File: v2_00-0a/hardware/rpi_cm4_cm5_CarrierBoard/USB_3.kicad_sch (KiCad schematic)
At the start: 90 parts, among them J2 0484050003, J3 0484050003, U5 UPD720202K8-711-BAA-A, U6 SST25VF512A, U7 UPD720202K8-711-BAA-A, U8 AP2192AFGEG-7, Y1 24MHz

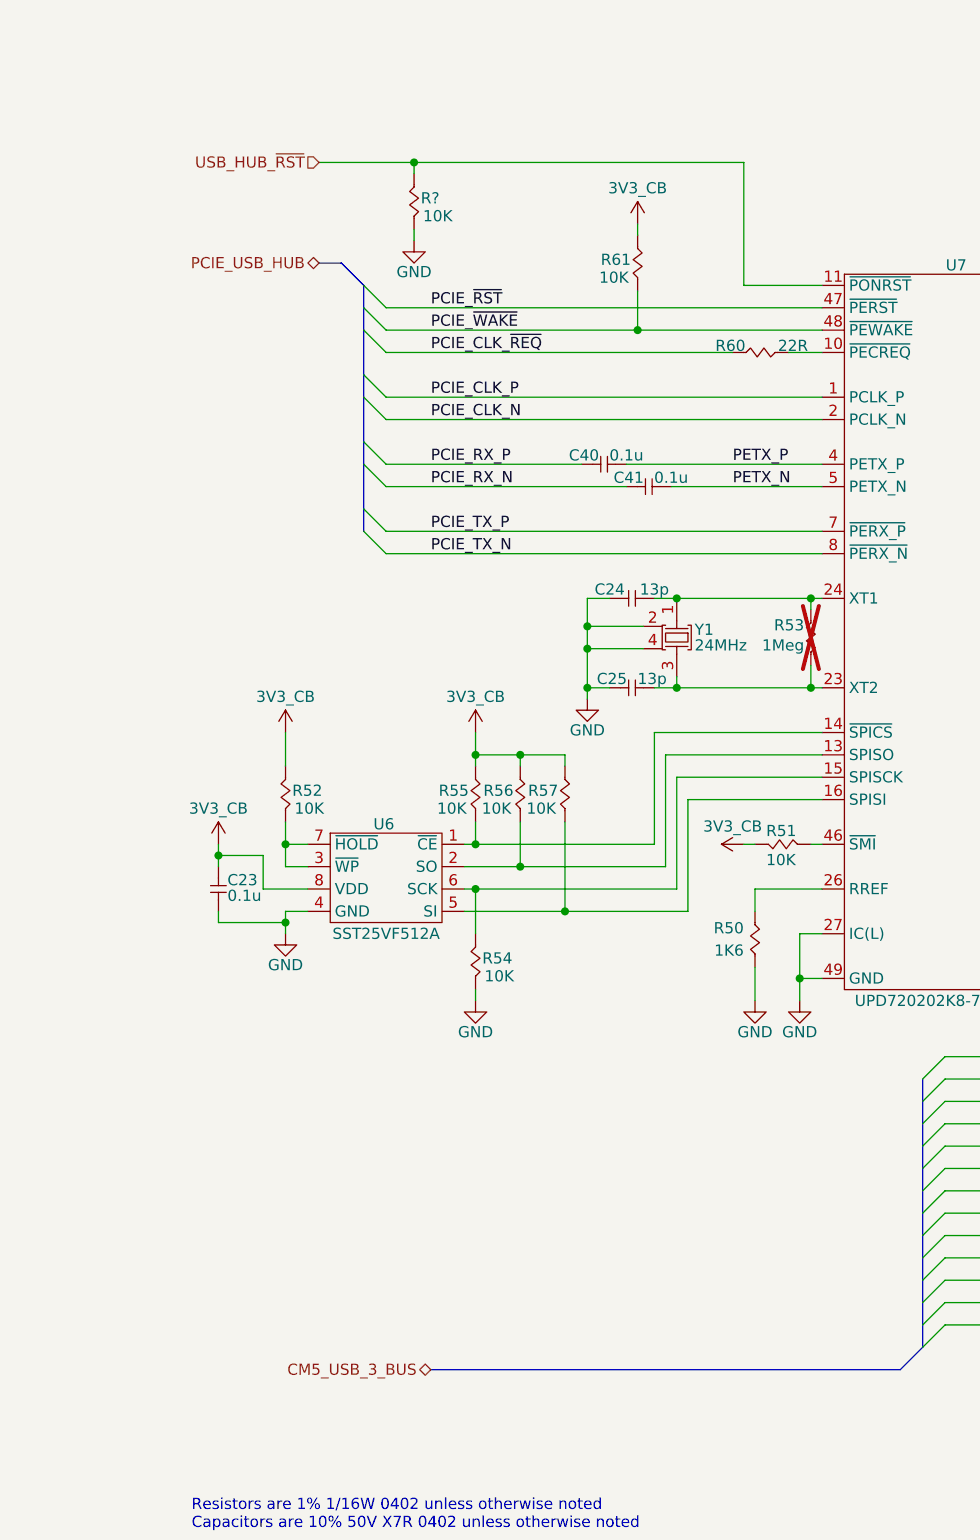
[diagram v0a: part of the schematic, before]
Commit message: Add schematic pages for SOM_CONN_A/B, DSI to LVDS bridge, Ethernet and HDMI
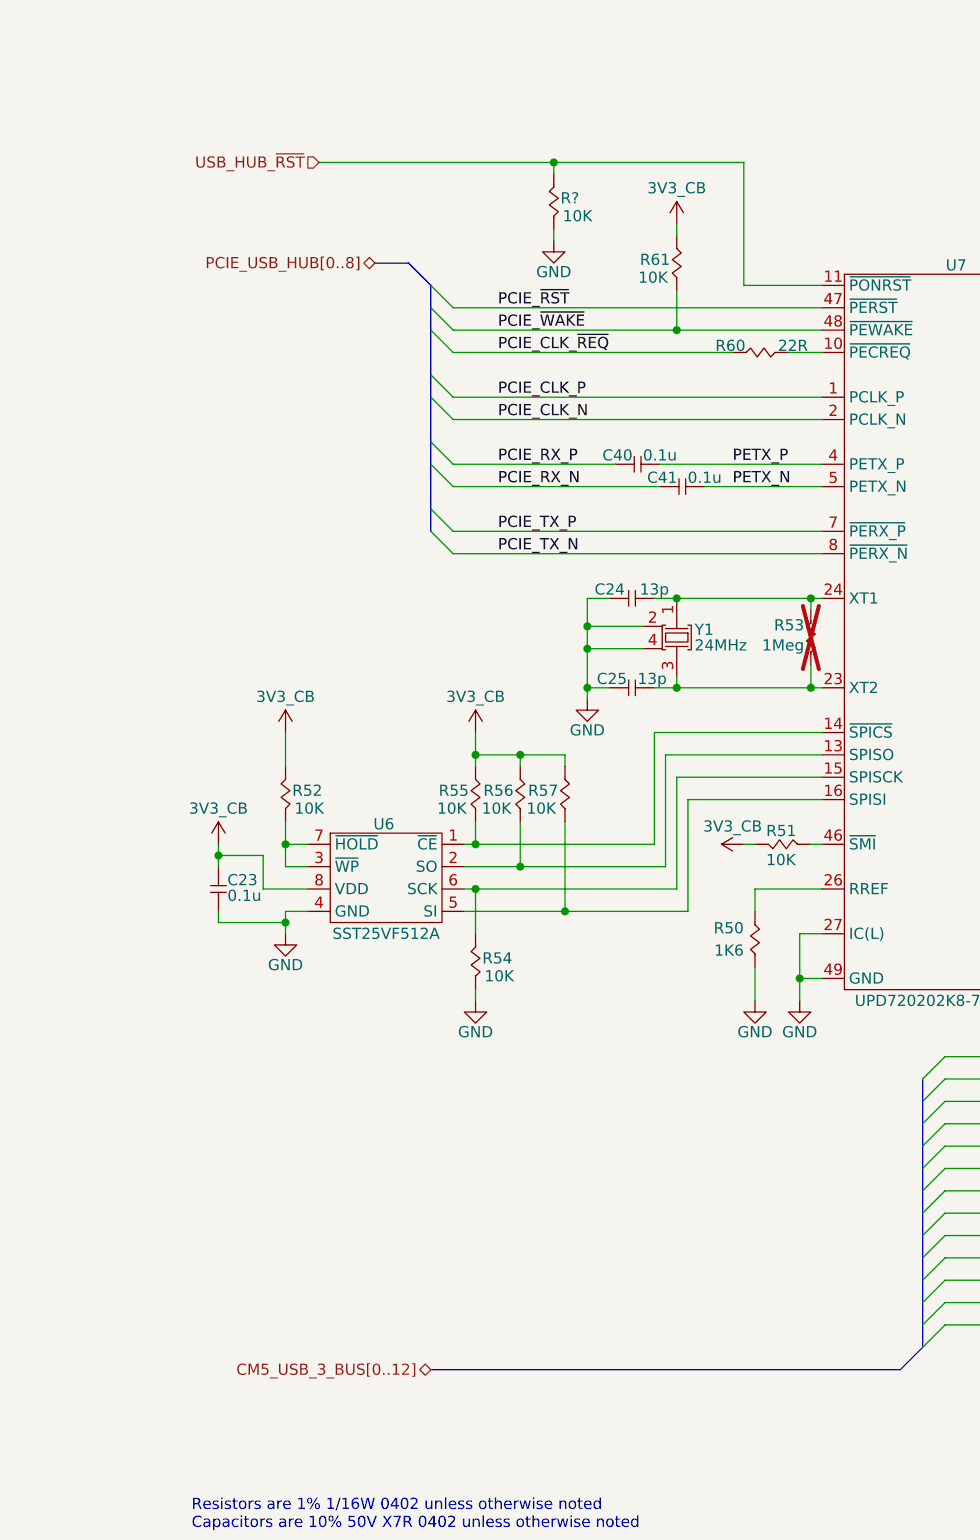
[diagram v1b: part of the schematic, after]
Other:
- moved on the sheet: C40, C41, R61, R?

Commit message: Update schematics (several new hierarchical pages, updates bus labels)
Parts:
- removed U5: UPD720202K8-711-BAA-A, footprint:48-VFQFN-EP, symbol KicadCompDb:Interface/INTRFX_00002
- added R128, R44: 0R, footprint:RES_0402, symbol KicadCompDb:Resistors/RES_SMT_00001
- gave numbers to parts that had none: 2
- renumbered R44 to R127
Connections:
- net CM5_USB3_VBUS_EN: now also R44.1; no longer R127.1
- net at R27.2, R49.1, U8.5 (FLG2): now also R128.2
- net at R26.2, R46.2, U8.3 (EN1): now also R44.2; no longer R127.2
- net at R25.2, R48.1, U8.8 (FLG1): now also R127.2
- net CM5_USB2_D1_N renamed CM5_USB3_0.USB_N
- net CM5_USB2_D1_P renamed CM5_USB3_0.USB_P
- net CM5_USB2_D2_N renamed CM5_USB3_1.USB_N
- net CM5_USB2_D2_P renamed CM5_USB3_1.USB_P
- net CM5_USB3_RX1_N renamed CM5_USB3_0.U3RXD_N
- net CM5_USB3_RX1_P renamed CM5_USB3_0.U3RXD_P
- net CM5_USB3_RX2_N renamed CM5_USB3_1.U3RXD_N
- net CM5_USB3_RX2_P renamed CM5_USB3_1.U3RXD_P
- net CM5_USB3_TX2_N renamed CM5_USB3_1.U3TXD_N
- net CM5_USB3_TX2_P renamed CM5_USB3_1.U3TXD_P
- net CM5_USB3_U3TX1_N renamed CM5_USB3_0.U3TXD_N
- net CM5_USB3_U3TX1_P renamed CM5_USB3_0.U3TXD_P
- net CONN_USB3_D1_N renamed USB3_0.USB_N
- net CONN_USB3_D1_P renamed USB3_0.USB_P
- net CONN_USB3_D2_N renamed USB3_1.USB_N
- net CONN_USB3_D2_P renamed USB3_1.USB_P
- net CONN_USB3_RX1_N renamed USB3_0.U3RXD_N
- net CONN_USB3_RX1_P renamed USB3_0.U3RXD_P
- net CONN_USB3_RX2_N renamed USB3_1.U3RXD_N
- net CONN_USB3_RX2_P renamed USB3_1.U3RXD_P
- net CONN_USB3_TX1_N renamed USB3_0.U3TXD_N
- net CONN_USB3_TX1_P renamed USB3_0.U3TXD_P
- net CONN_USB3_TX2_N renamed USB3_1.U3TXD_N
- net CONN_USB3_TX2_P renamed USB3_1.U3TXD_P
- net USB3_0_VBUS renamed USB3_0.USB_VBUS
- net USB3_1_VBUS renamed USB3_1.USB_VBUS
- new net CM5_USB3_0_~{OC}: R127.1
- new net CM5_USB3_1_~{OC}: R128.1
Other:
- moved on the sheet: R127, R46, R47, R48, R49, R53

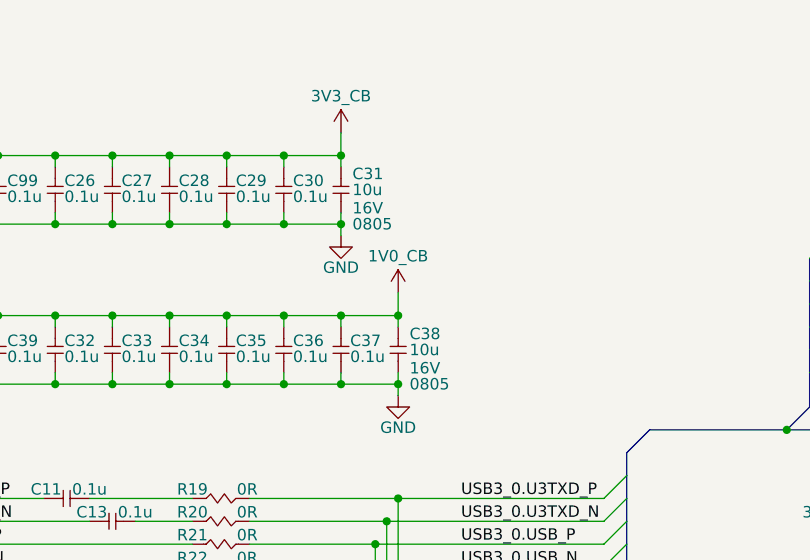
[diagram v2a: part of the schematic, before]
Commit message: Add new page and update schematics
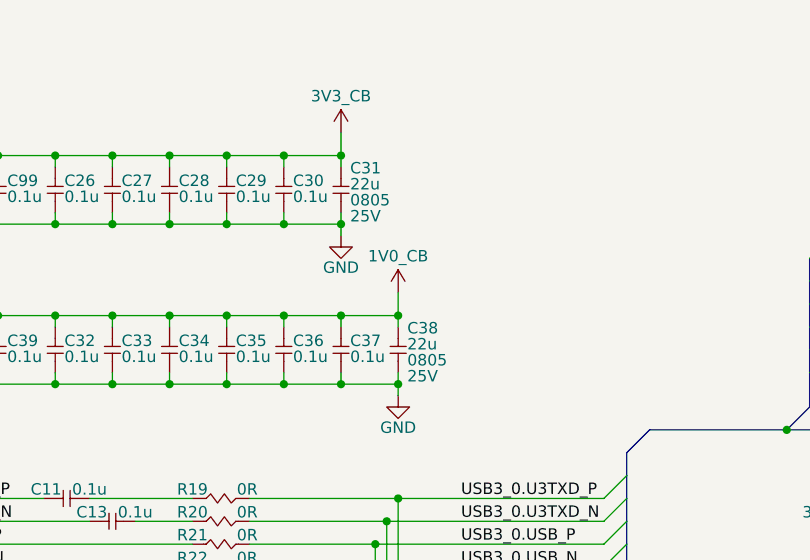
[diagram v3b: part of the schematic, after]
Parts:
- removed C31, C38: 10u, footprint:CAP_NONPOL_0805, symbol KicadCompDb:Capacitors/CAP_CER_SMT_00004
- added C31, C38: 22u, footprint:CAP_NONPOL_0805, symbol KicadCompDb:Capacitors/CAP_CER_SMT_00011
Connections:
- net 1V0_CB: now also C38.2
- net 3V3_CB: now also C31.2
- net GND: now also C31.1, C38.1

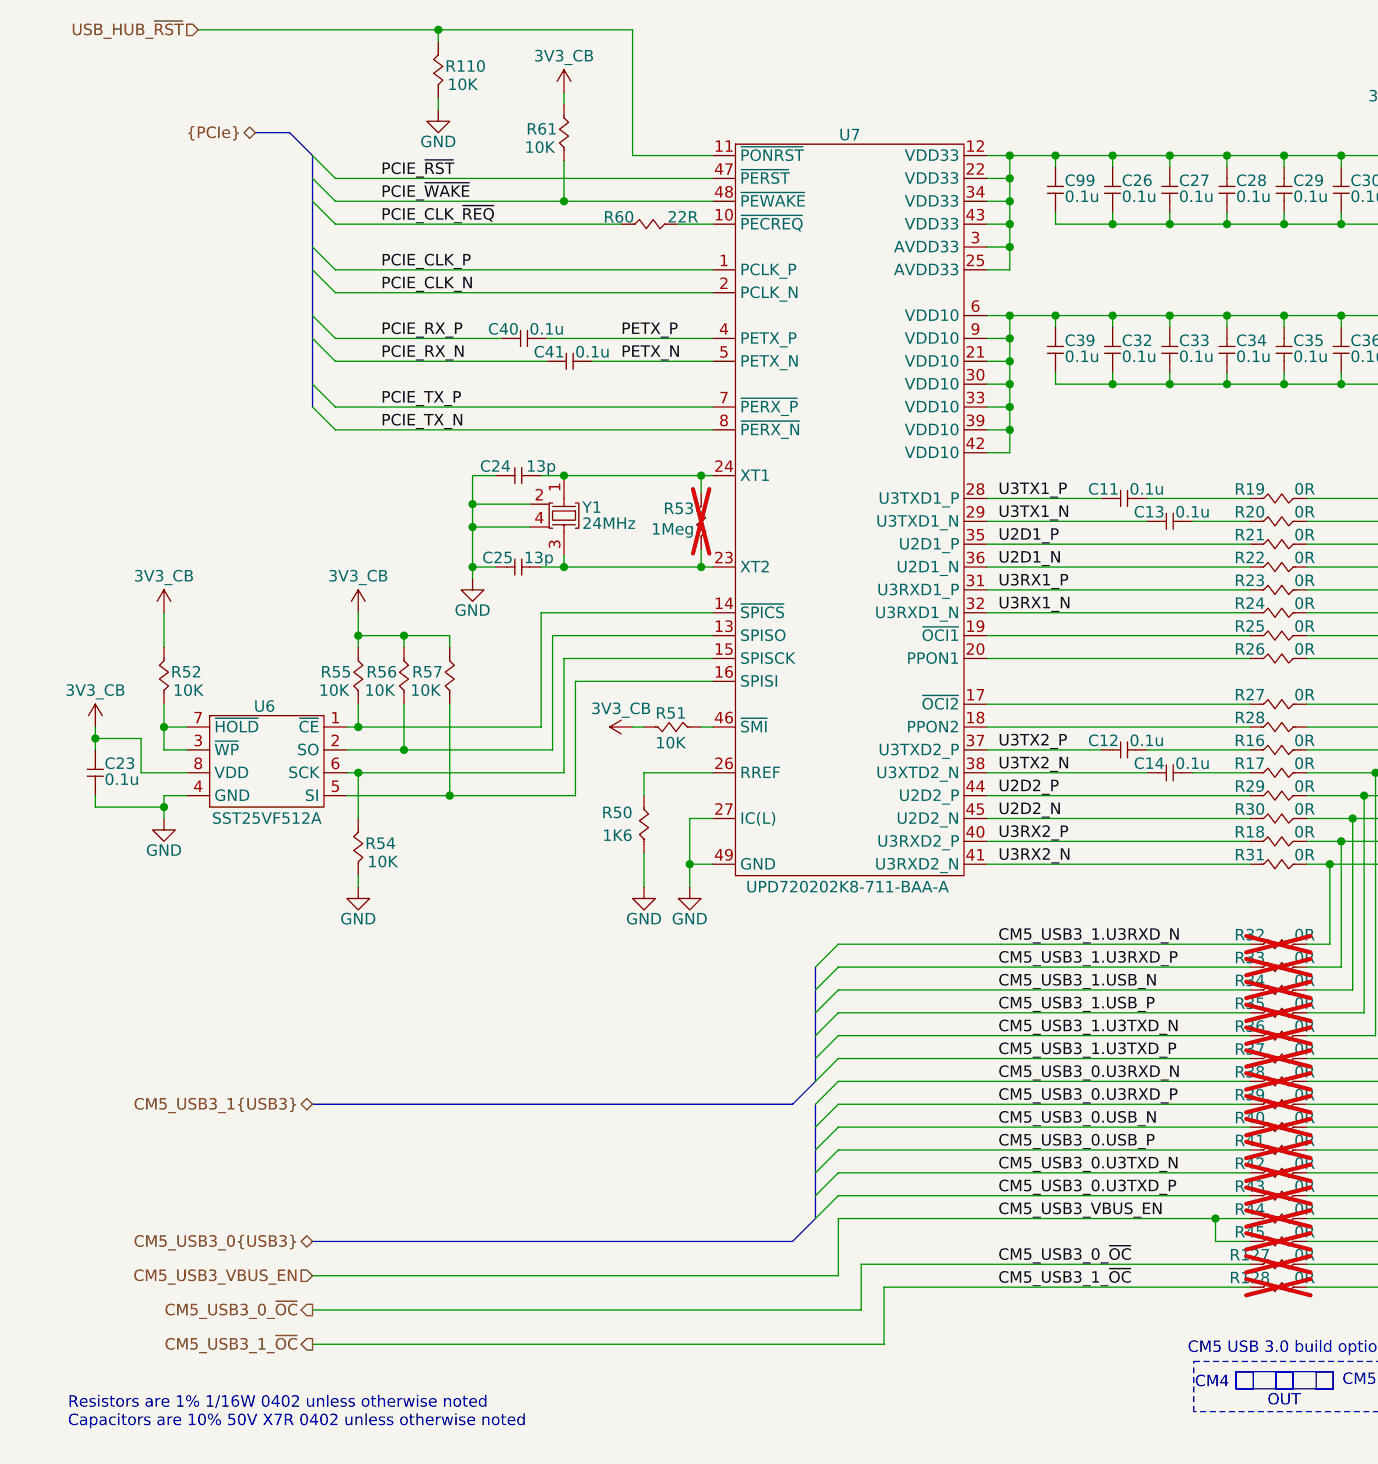
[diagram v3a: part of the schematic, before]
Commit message: Add design notes (power table) and latest changes to power supply and power input
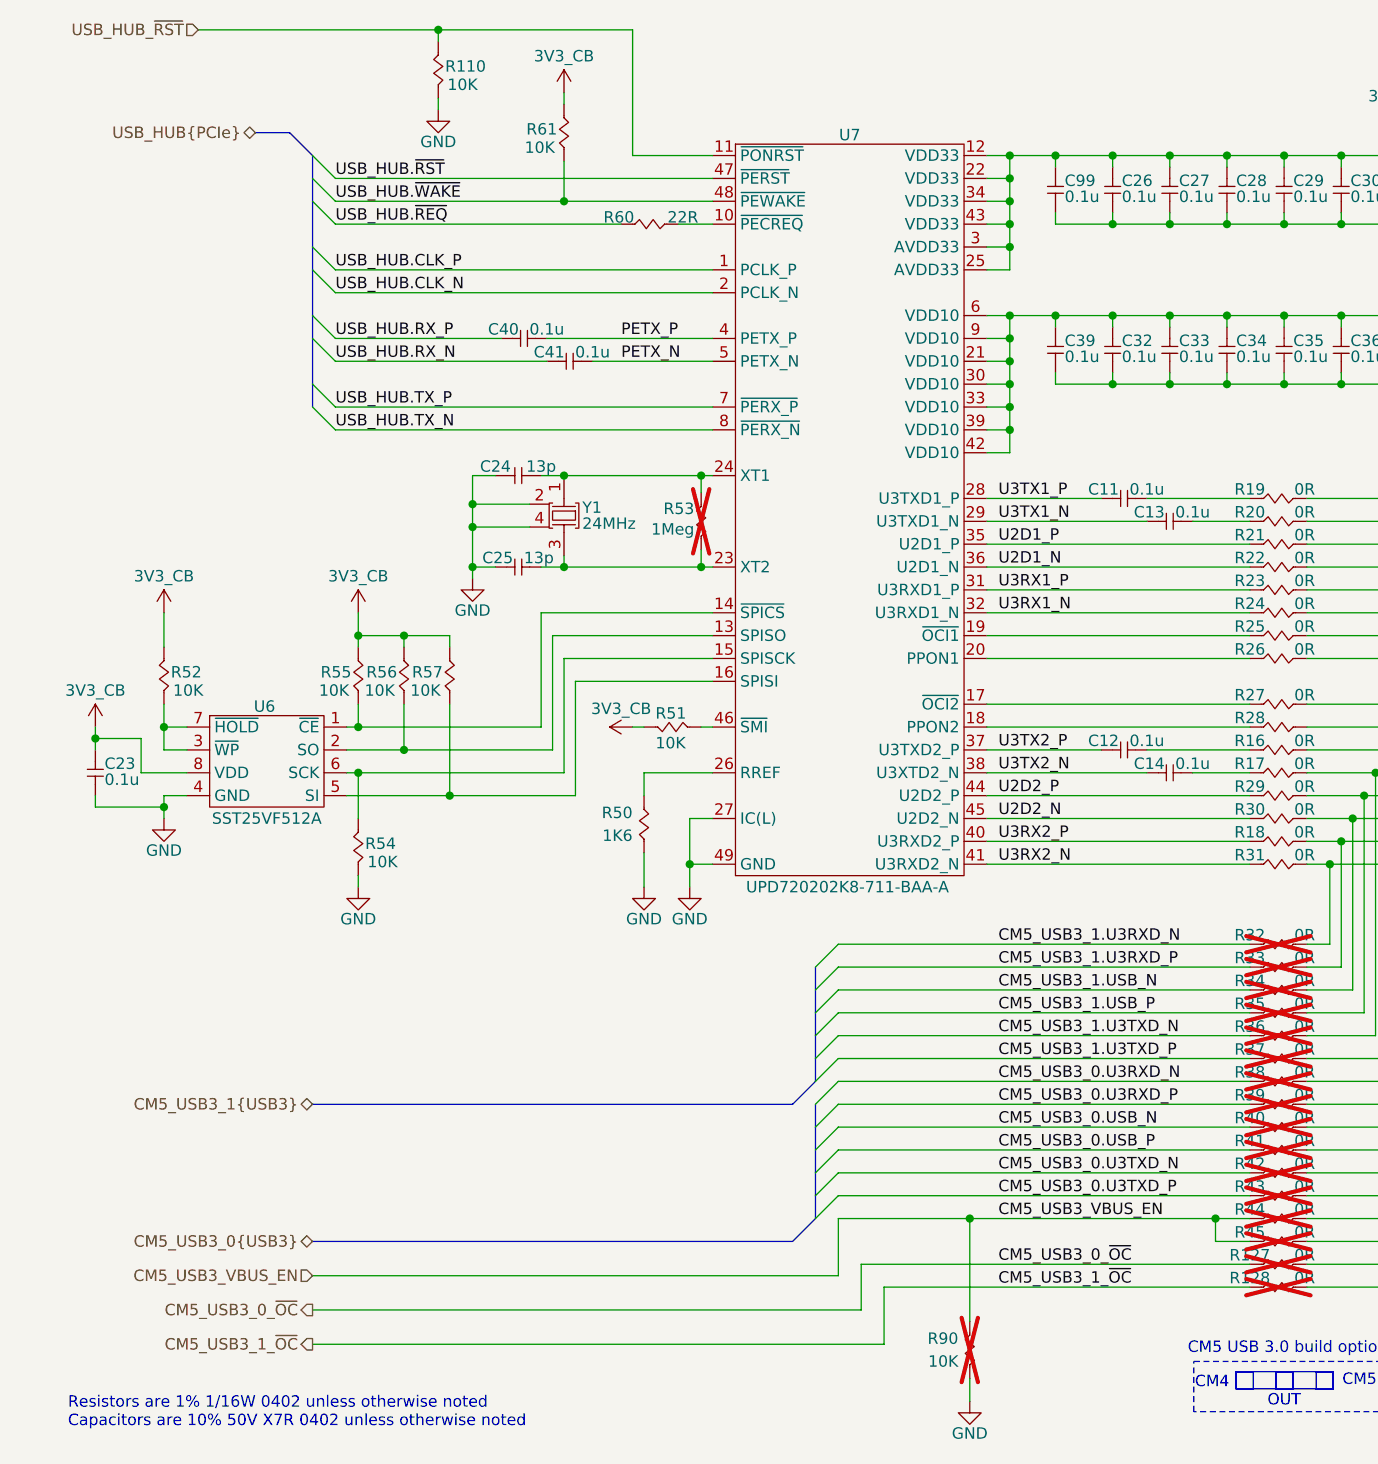
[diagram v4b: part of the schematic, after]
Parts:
- added R90: 10K, footprint:RES_0402, symbol KicadCompDb:Resistors/RES_SMT_00013
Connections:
- net CM5_USB3_VBUS_EN: now also R90.2
- net GND: now also R90.1
- net PCIE_CLK_N renamed USB_HUB.CLK_N
- net PCIE_CLK_P renamed USB_HUB.CLK_P
- net PCIE_CLK_~{REQ} renamed USB_HUB.~{REQ}
- net PCIE_RX_N renamed USB_HUB.RX_N
- net PCIE_RX_P renamed USB_HUB.RX_P
- net PCIE_TX_N renamed USB_HUB.TX_N
- net PCIE_TX_P renamed USB_HUB.TX_P
- net PCIE_~{RST} renamed USB_HUB.~{RST}
- net PCIE_~{WAKE} renamed USB_HUB.~{WAKE}

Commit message: Add and modify existing schematics
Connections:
- net 1V0_CB renamed 1V05_CB
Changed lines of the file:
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@@
 			)
 		)
-		(property "Value" "1V0_CB"
+		(property "Value" "1V05_CB"
 			(at 167.64 41.656 0)
 			(effects
